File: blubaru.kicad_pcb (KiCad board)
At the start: 2 copper layers, 80 x 78.7 mm, 68 parts, among them IC1 ATTINY4313-P, J1 DB15, J2 DB15, J3 TS5A22364-Q1, J4 TS5A22364-Q1, J5 RN52_BREAKOUT, J6 JACK_TRS_5PINS, J7 DRV632, J8 JACK_TRS_5PINS, P1 CONN_01X06, P2 CONN_02X03, SW1 SW_Push, U1 DG419, U2 LD1117V33, Y1 11.0592MHz

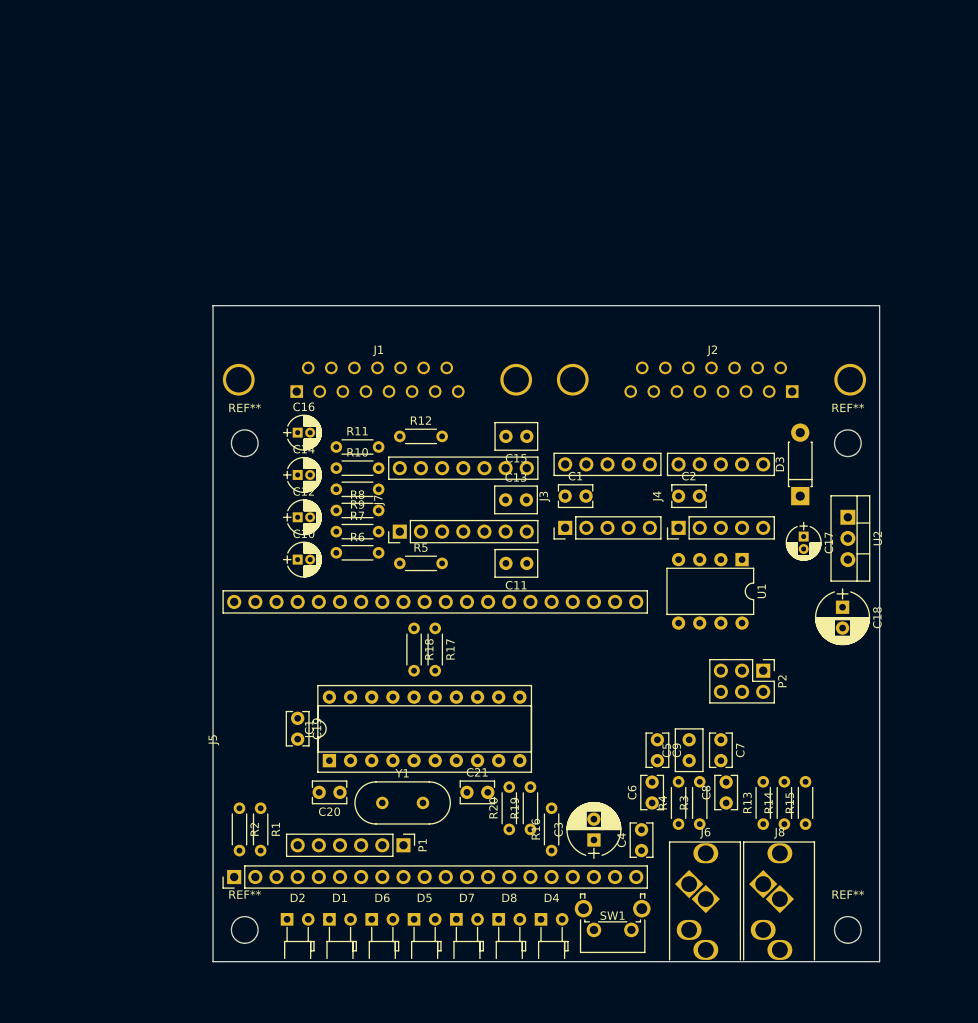
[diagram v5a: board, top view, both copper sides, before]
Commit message: Power and audio paths connected.
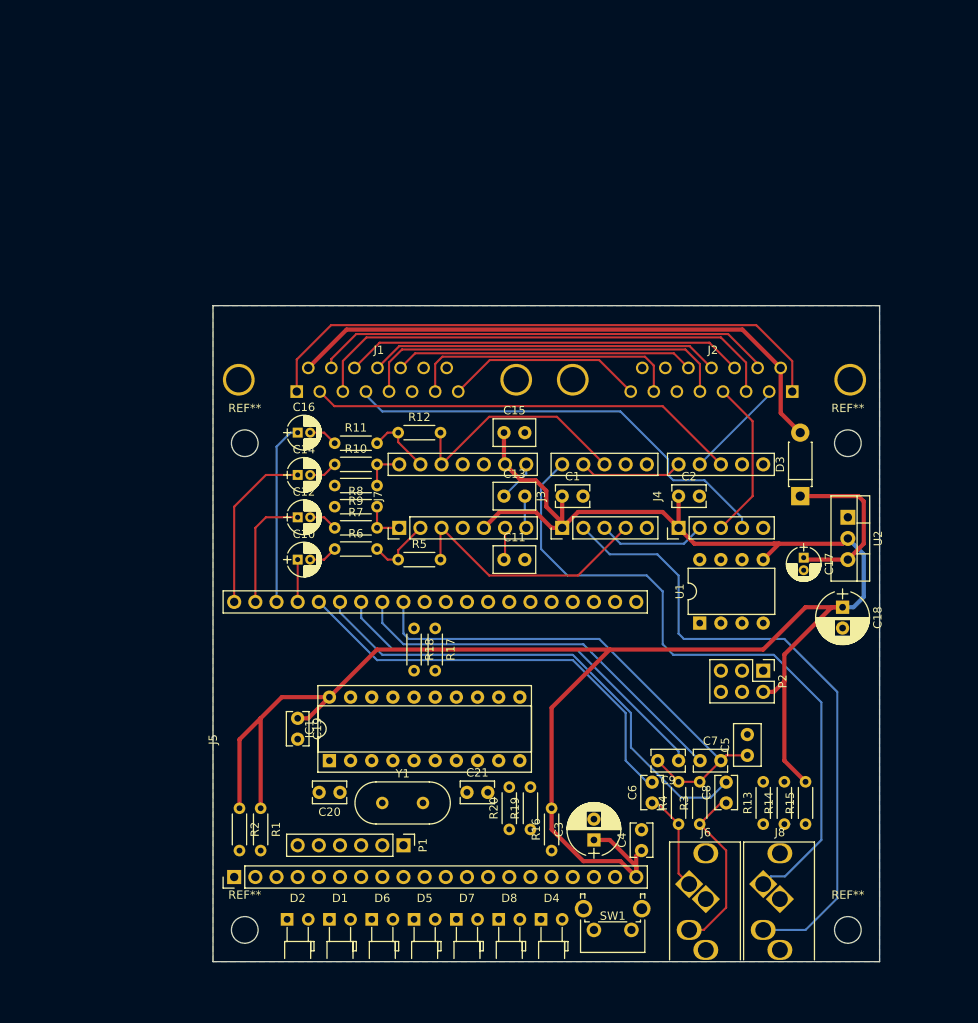
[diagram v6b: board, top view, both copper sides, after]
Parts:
- moved U1 9.16 mm to (166.4, 99.1), turned to 90 degrees
- moved C5 7.01 mm to (172.1, 114.9)
- moved C9 3.56 mm to (163.8, 115.6), turned to 180 degrees
- moved C7 3.54 mm to (166.4, 115.6), turned to 0 degrees
- moved C11 2.77 mm to (142.9, 91.4), turned to 0 degrees
- moved C15 2.77 mm to (142.9, 76.2), turned to 0 degrees
- moved C17 2.54 mm to (178.8, 91.2)
- moved C13 0.49 mm to (142.9, 83.8)
- moved R10 0.49 mm to (122.6, 80.0)
- moved R11 0.49 mm to (122.6, 77.5)
- moved R12 0.49 mm to (130.2, 76.2)
- moved R5 0.49 mm to (130.2, 91.4)
- moved R6 0.49 mm to (122.6, 90.2)
- moved R7 0.49 mm to (122.6, 87.6)
- moved R8 0.49 mm to (122.6, 85.1)
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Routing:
- net VCC: track 0.00 -> 264.8 mm
- net /DB-15 interconnects/Modules/Audio switch/LINE_R: track 0.00 -> 81.9 mm
- net /DB-15 interconnects/Modules/Audio switch/LINE_L: track 0.00 -> 78.6 mm
- net /DB-15 interconnects/1_IN: track 0.00 -> 70.5 mm
- net +12V: track 0.00 -> 69.3 mm
- net /DB-15 interconnects/Modules/Bluetooth Module/Microphone/MIC_BIAS: track 0.00 -> 61.4 mm
- net /DB-15 interconnects/Modules/Bluetooth Module/Microphone/MIC_L-: track 0.00 -> 60.0 mm
- net /DB-15 interconnects/3_IN: track 0.00 -> 58.0 mm
- net /DB-15 interconnects/10_IN: track 0.00 -> 55.5 mm
- net /DB-15 interconnects/4_IN: track 0.00 -> 54.0 mm
- net /DB-15 interconnects/Modules/Bluetooth Module/Microphone/MIC_R-: track 0.00 -> 52.3 mm
- net /DB-15 interconnects/2_IN: track 0.00 -> 51.8 mm
- net /DB-15 interconnects/11_IN: track 0.00 -> 48.1 mm
- net /DB-15 interconnects/Modules/Bluetooth Module/Microphone/MIC_R+: track 0.00 -> 47.8 mm
- net /DB-15 interconnects/Modules/Bluetooth Module/Microphone/MIC_L+: track 0.00 -> 47.5 mm
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- added copper zone on B.Cu, net GND
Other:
- net class Power: trace_width 0.3048 -> 0.508

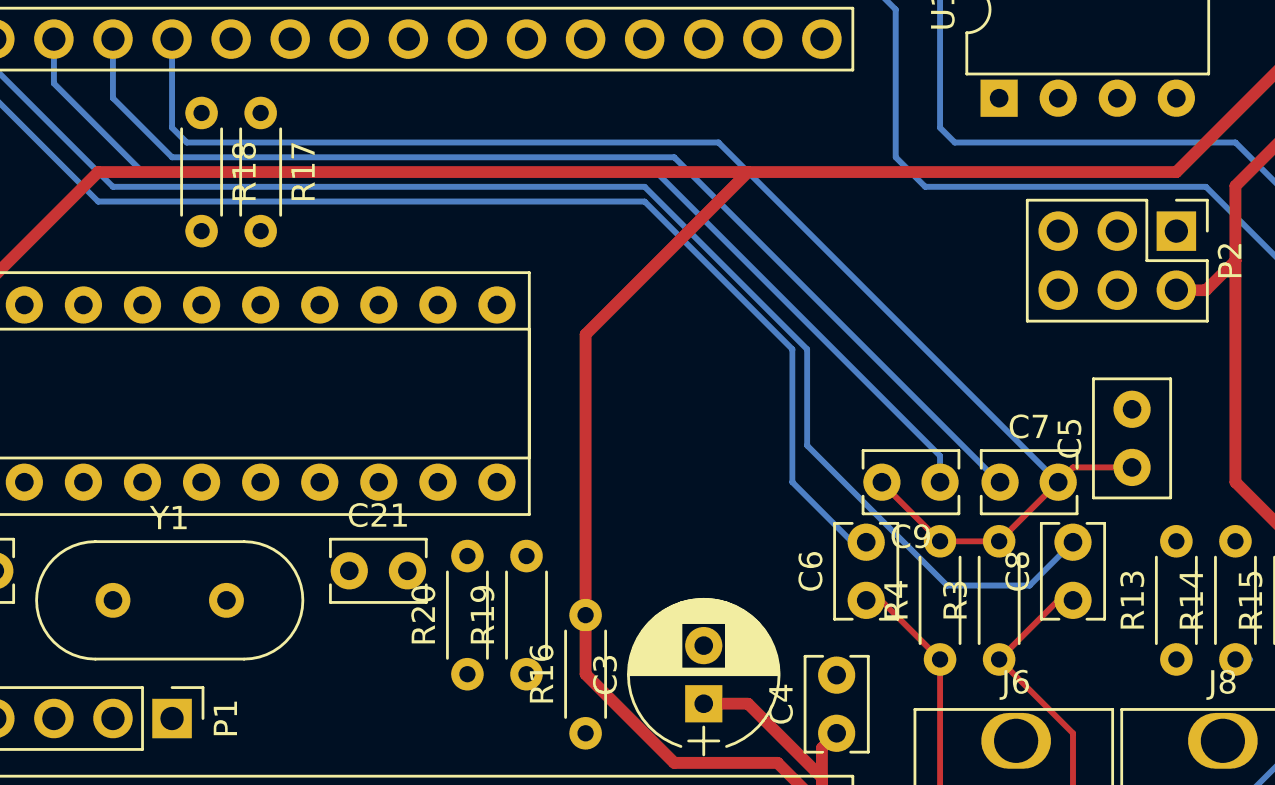
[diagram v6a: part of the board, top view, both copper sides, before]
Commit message: Fixup mic jack parts after schematic change (rebase).
Some parts got flipped in 04f718b, onto which subsequent comments got rebased
later.
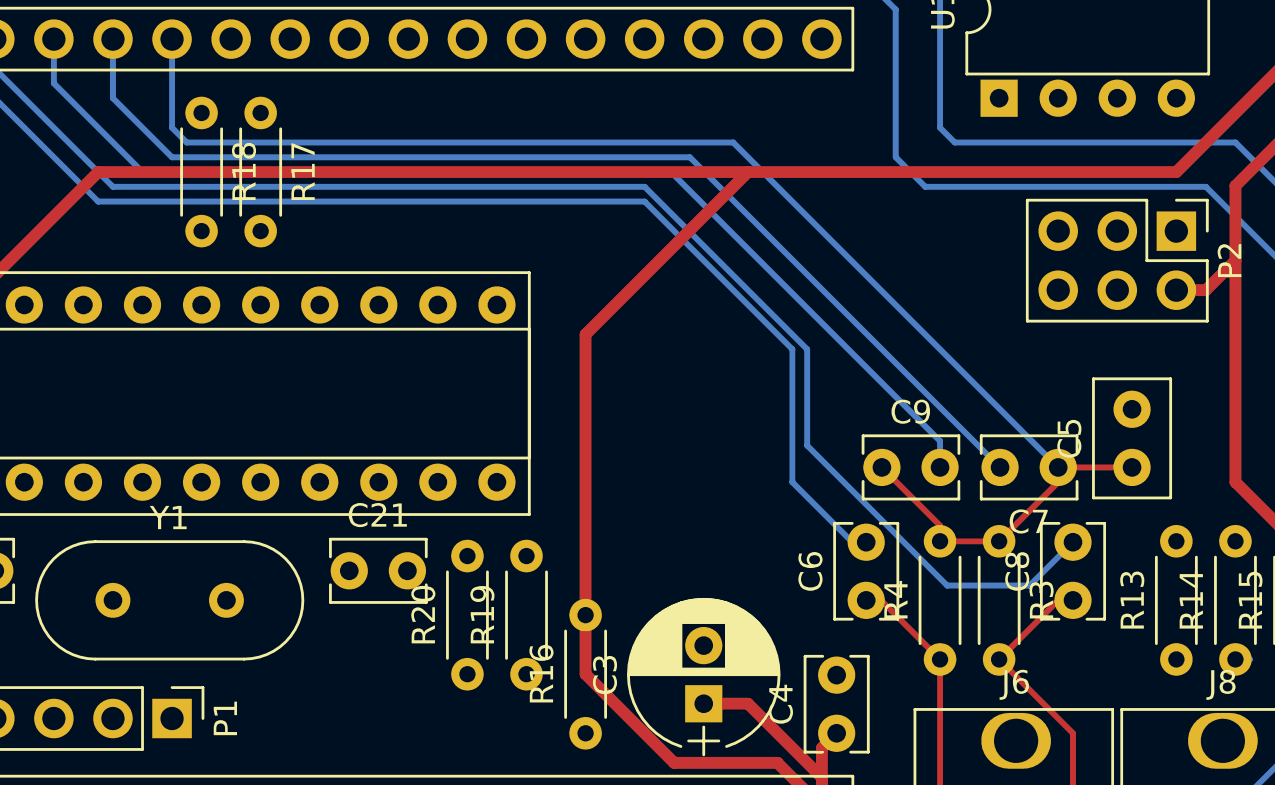
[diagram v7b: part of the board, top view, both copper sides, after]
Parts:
- moved R3 5.08 mm to (166.4, 118.1), turned to 270 degrees
- moved C7 2.58 mm to (168.9, 114.9), turned to 180 degrees
- moved C9 2.58 mm to (161.3, 114.9), turned to 0 degrees
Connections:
- C17 pad 1: Net-(C17-Pad1) -> +12V
- C7 pad 1: /DB-15 interconnects/Modules/Bluetooth Module/Microphone/MIC_L+ -> /DB-15 interconnects/Modules/Bluetooth Module/Microphone/MIC_BIAS
- C7 pad 2: /DB-15 interconnects/Modules/Bluetooth Module/Microphone/MIC_BIAS -> /DB-15 interconnects/Modules/Bluetooth Module/Microphone/MIC_L+
- C9 pad 1: /DB-15 interconnects/Modules/Bluetooth Module/Microphone/MIC_R+ -> /DB-15 interconnects/Modules/Bluetooth Module/Microphone/MIC_BIAS
- C9 pad 2: /DB-15 interconnects/Modules/Bluetooth Module/Microphone/MIC_BIAS -> /DB-15 interconnects/Modules/Bluetooth Module/Microphone/MIC_R+
- D3 pad 1: Net-(C17-Pad1) -> +12V
- D3 pad 2: +12V -> +BATT
- J1 pad 9: +12V -> +BATT
- J2 pad 9: +12V -> +BATT
- R3 pad 1: Net-(C8-Pad1) -> /DB-15 interconnects/Modules/Bluetooth Module/Microphone/MIC_BIAS
- R3 pad 2: /DB-15 interconnects/Modules/Bluetooth Module/Microphone/MIC_BIAS -> Net-(C8-Pad1)
- U2 pad 3: Net-(C17-Pad1) -> +12V
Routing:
- net +BATT: track 0.00 -> 69.3 mm
- net +12V: track 69.3 -> 21.1 mm
- net Net-(C17-Pad1): track 21.1 -> 0.00 mm
- net /DB-15 interconnects/Modules/Bluetooth Module/Microphone/MIC_BIAS: track 61.4 -> 63.1 mm
- net /DB-15 interconnects/Modules/Bluetooth Module/Microphone/MIC_R+: track 47.8 -> 48.6 mm

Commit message: Update net names, re-arrange LEDs
Separated the RESET and BT_RESET nets. They collided previously.
Renamed components after a few things shifted around.
Moved LEDs around so they are in order.
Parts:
- moved D1 30.5 mm to (116.8, 134.6)
- moved D7 30.5 mm to (147.3, 134.6)
- moved D2 20.3 mm to (121.9, 134.6)
- moved D6 20.3 mm to (142.2, 134.6)
- renumbered C9 to C7, C7 to C8, C8 to C9, D4 to D1, D8 to D2, D6 to D3, D5 to D4, D7 to D5, D1 to D6, D2 to D7, D3 to D8, R20 to R17, R17 to R19, R19 to R20, R4 to R3, R3 to R4
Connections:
- IC1 pad 1: /DB-15 interconnects/Modules/Bluetooth Module/RESET -> /DB-15 interconnects/Modules/Microcontroller/RESET
- IC1 pad 11: /DB-15 interconnects/Modules/Bluetooth Module/RESET -> /DB-15 interconnects/Modules/Microcontroller/BT_RESET
- J1 pad 15: (no net) -> Net-(J1-Pad15)
- J2 pad 15: (no net) -> Net-(J2-Pad15)
- J5 pad 1: /DB-15 interconnects/Modules/Bluetooth Module/RESET -> /DB-15 interconnects/Modules/Microcontroller/BT_RESET
- J5 pad 11: (no net) -> Net-(J5-Pad11)
- J5 pad 12: (no net) -> Net-(J5-Pad12)
- J5 pad 13: (no net) -> Net-(J5-Pad13)
- J5 pad 14: (no net) -> Net-(J5-Pad14)
- J5 pad 18: (no net) -> Net-(J5-Pad18)
- J5 pad 22: (no net) -> Net-(J5-Pad22)
- J5 pad 23: (no net) -> Net-(J5-Pad23)
- J5 pad 24: (no net) -> Net-(J5-Pad24)
- J5 pad 25: (no net) -> Net-(J5-Pad25)
- J5 pad 26: (no net) -> Net-(J5-Pad26)
- J5 pad 27: (no net) -> Net-(J5-Pad27)
- J5 pad 28: (no net) -> Net-(J5-Pad28)
- J5 pad 29: (no net) -> Net-(J5-Pad29)
- J5 pad 3: (no net) -> Net-(J5-Pad3)
- J5 pad 4: (no net) -> Net-(J5-Pad4)
- J6 pad 4: (no net) -> Net-(J6-Pad4)
- J6 pad 5: (no net) -> Net-(J6-Pad5)
- J7 pad 11: (no net) -> Net-(J7-Pad11)
- J8 pad 5: (no net) -> Net-(J8-Pad5)
- P2 pad 5: /DB-15 interconnects/Modules/Bluetooth Module/RESET -> /DB-15 interconnects/Modules/Microcontroller/RESET
- SW1 pad 2: /DB-15 interconnects/Modules/Bluetooth Module/RESET -> /DB-15 interconnects/Modules/Microcontroller/RESET
